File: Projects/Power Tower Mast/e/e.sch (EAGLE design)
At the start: 25 parts

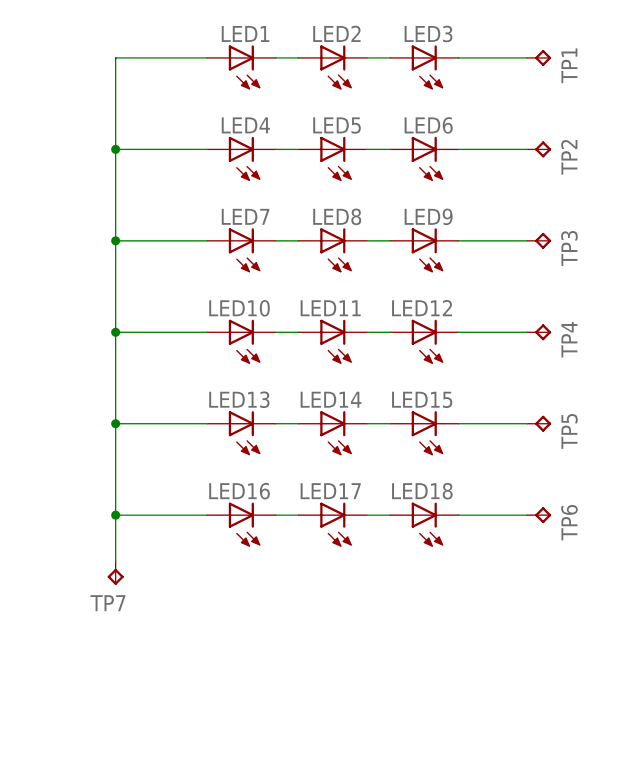
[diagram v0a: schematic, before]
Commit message: updated with extra vias and panelized
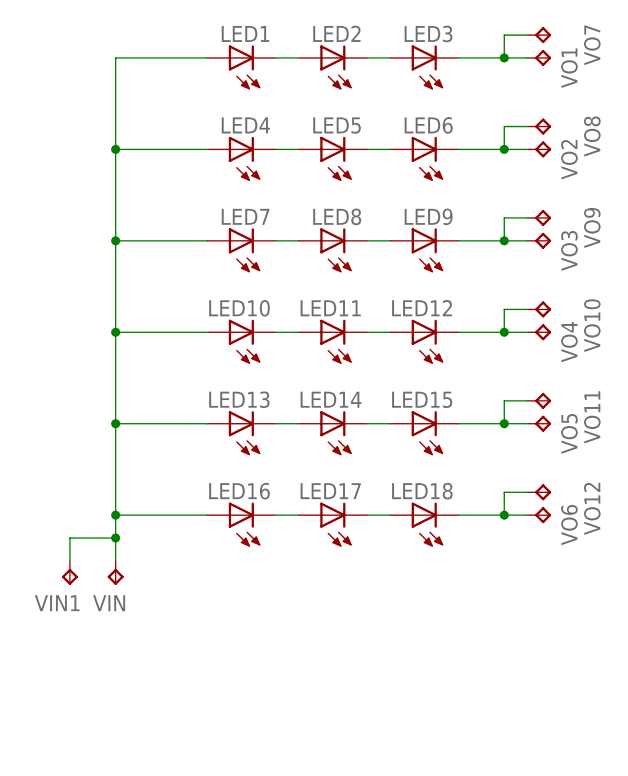
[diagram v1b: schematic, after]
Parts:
- added VIN1, VO10, VO11, VO12, VO7, VO8, VO9: (no value), CyberRailGuru:TEST_POINTPAD1-20
- renumbered TP1 to VO1, TP2 to VO2, TP3 to VO3, TP4 to VO4, TP5 to VO5, TP6 to VO6, TP7 to VIN
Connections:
- removed net VIN4: LED1.A, LED10.A, LED13.A, LED16.A, LED4.A, LED7.A, VIN.TP
- removed net VOUT20: LED3.C, VO1.TP
- removed net VOUT21: LED6.C, VO2.TP
- removed net VOUT22: LED9.C, VO3.TP
- removed net VOUT23: LED12.C, VO4.TP
- removed net VOUT24: LED15.C, VO5.TP
- removed net VOUT25: LED18.C, VO6.TP
- new net VIN: LED1.A, LED10.A, LED13.A, LED16.A, LED4.A, LED7.A, VIN.TP, VIN1.TP
- new net VOUT1: LED3.C, VO1.TP, VO7.TP
- new net VOUT2: LED6.C, VO2.TP, VO8.TP
- new net VOUT3: LED9.C, VO3.TP, VO9.TP
- new net VOUT4: LED12.C, VO10.TP, VO4.TP
- new net VOUT5: LED15.C, VO11.TP, VO5.TP
- new net VOUT6: LED18.C, VO12.TP, VO6.TP

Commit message: reworking some letters
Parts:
- added LED19, LED20, LED21: (no value), CyberRailGuru:LED0805
- added VO13, VO14: (no value), CyberRailGuru:TEST_POINTPAD1-20
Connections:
- new net N$1: LED19.C, LED20.A
- new net N$2: LED20.C, LED21.A
- new net N$3: LED21.C, VO14.TP, VO7.TP
- net VIN: now also LED19.A
- net VOUT1: now also VO8.TP; no longer VO7.TP
- net VOUT2: now also VO9.TP; no longer VO8.TP
- net VOUT3: now also VO10.TP; no longer VO9.TP
- net VOUT4: now also VO11.TP; no longer VO10.TP
- net VOUT5: now also VO12.TP; no longer VO11.TP
- net VOUT6: now also VO13.TP; no longer VO12.TP
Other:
- moved on the sheet: VIN, VIN1, VO10, VO11, VO12, VO7, VO8, VO9
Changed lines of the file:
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@@
 <part name="VO6" library="CyberRailGuru" deviceset="TEST_POINT" device="PAD1-20"/>
 <part name="VIN1" library="CyberRailGuru" deviceset="TEST_POINT" device="PAD1-20"/>
-<part name="VO7" library="CyberRailGuru" deviceset="TEST_POINT" device="PAD1-20"/>
 <part name="VO8" library="CyberRailGuru" deviceset="TEST_POINT" device="PAD1-20"/>
 <part name="VO9" library="CyberRailGuru" deviceset="TEST_POINT" device="PAD1-20"/>
@@
 <part name="VO11" library="CyberRailGuru" deviceset="TEST_POINT" device="PAD1-20"/>
 <part name="VO12" library="CyberRailGuru" deviceset="TEST_POINT" device="PAD1-20"/>
+<part name="VO13" library="CyberRailGuru" deviceset="TEST_POINT" device="PAD1-20"/>
+<part name="LED19" library="CyberRailGuru" deviceset="LED" device="0805"/>
+<part name="LED20" library="CyberRailGuru" deviceset="LED" device="0805"/>
+<part name="LED21" library="CyberRailGuru" deviceset="LED" device="0805"/>
+<part name="VO7" library="CyberRailGuru" deviceset="TEST_POINT" device="PAD1-20"/>
+<part name="VO14" library="CyberRailGuru" deviceset="TEST_POINT" device="PAD1-20"/>
 </parts>
 <sheets>
@@
 <instance part="LED17" gate="G$1" x="81.28" y="144.78" rot="R90"/>
 <instance part="LED16" gate="G$1" x="71.12" y="144.78" rot="R90"/>
-<instance part="VIN" gate="G$1" x="58.42" y="137.16" rot="R180"/>
+<instance part="VIN" gate="G$1" x="58.42" y="121.92" rot="R180"/>
 <instance part="VO1" gate="G$1" x="106.68" y="195.58" smashed="yes" rot="R270">
 <attribute name="NAME" x="107.95" y="196.85" size="1.778" layer="95" rot="R270"/>
@@
 <attribute name="VALUE" x="105.41" y="143.51" size="1.778" layer="96" rot="R270"/>
 </instance>
-<instance part="VIN1" gate="G$1" x="53.34" y="137.16" rot="R180"/>
-<instance part="VO7" gate="G$1" x="106.68" y="198.12" smashed="yes" rot="R270">
+<instance part="VIN1" gate="G$1" x="53.34" y="121.92" rot="R180"/>
+<instance part="VO8" gate="G$1" x="106.68" y="198.12" smashed="yes" rot="R270">
 <attribute name="NAME" x="110.49" y="199.39" size="1.778" layer="95" rot="R270"/>
 <attribute name="VALUE" x="105.41" y="196.85" size="1.778" layer="96" rot="R270"/>
 </instance>
-<instance part="VO8" gate="G$1" x="106.68" y="187.96" smashed="yes" rot="R270">
+<instance part="VO9" gate="G$1" x="106.68" y="187.96" smashed="yes" rot="R270">
 <attribute name="NAME" x="110.49" y="189.23" size="1.778" layer="95" rot="R270"/>
 <attribute name="VALUE" x="105.41" y="186.69" size="1.778" layer="96" rot="R270"/>
 </instance>
-<instance part="VO9" gate="G$1" x="106.68" y="177.8" smashed="yes" rot="R270">
+<instance part="VO10" gate="G$1" x="106.68" y="177.8" smashed="yes" rot="R270">
 <attribute name="NAME" x="110.49" y="179.07" size="1.778" layer="95" rot="R270"/>
 <attribute name="VALUE" x="105.41" y="176.53" size="1.778" layer="96" rot="R270"/>
 </instance>
-<instance part="VO10" gate="G$1" x="106.68" y="167.64" smashed="yes" rot="R270">
+<instance part="VO11" gate="G$1" x="106.68" y="167.64" smashed="yes" rot="R270">
 <attribute name="NAME" x="110.49" y="168.91" size="1.778" layer="95" rot="R270"/>
 <attribute name="VALUE" x="105.41" y="166.37" size="1.778" layer="96" rot="R270"/>
 </instance>
-<instance part="VO11" gate="G$1" x="106.68" y="157.48" smashed="yes" rot="R270">
+<instance part="VO12" gate="G$1" x="106.68" y="157.48" smashed="yes" rot="R270">
 <attribute name="NAME" x="110.49" y="158.75" size="1.778" layer="95" rot="R270"/>
 <attribute name="VALUE" x="105.41" y="156.21" size="1.778" layer="96" rot="R270"/>
 </instance>
-<instance part="VO12" gate="G$1" x="106.68" y="147.32" smashed="yes" rot="R270">
+<instance part="VO13" gate="G$1" x="106.68" y="147.32" smashed="yes" rot="R270">
 <attribute name="NAME" x="110.49" y="148.59" size="1.778" layer="95" rot="R270"/>
 <attribute name="VALUE" x="105.41" y="146.05" size="1.778" layer="96" rot="R270"/>
+</instance>
+<instance part="LED19" gate="G$1" x="71.12" y="134.62" rot="R90"/>
+<instance part="LED20" gate="G$1" x="81.28" y="134.62" rot="R90"/>
+<instance part="LED21" gate="G$1" x="91.44" y="134.62" rot="R90"/>
+<instance part="VO7" gate="G$1" x="106.68" y="134.62" smashed="yes" rot="R270">
+<attribute name="NAME" x="107.95" y="135.89" size="1.778" layer="95" rot="R270"/>
+<attribute name="VALUE" x="105.41" y="133.35" size="1.778" layer="96" rot="R270"/>
+</instance>
+<instance part="VO14" gate="G$1" x="106.68" y="137.16" smashed="yes" rot="R270">
+<attribute name="NAME" x="110.49" y="138.43" size="1.778" layer="95" rot="R270"/>
+<attribute name="VALUE" x="105.41" y="135.89" size="1.778" layer="96" rot="R270"/>
 </instance>
 </instances>
@@
 <wire x1="96.52" y1="195.58" x2="101.6" y2="195.58" width="0.1524" layer="91"/>
 <pinref part="VO1" gate="G$1" pin="TP"/>
-<pinref part="VO7" gate="G$1" pin="TP"/>
+<pinref part="VO8" gate="G$1" pin="TP"/>
 <wire x1="101.6" y1="195.58" x2="104.14" y2="195.58" width="0.1524" layer="91"/>
 <wire x1="104.14" y1="198.12" x2="101.6" y2="198.12" width="0.1524" layer="91"/>
@@
 <wire x1="96.52" y1="185.42" x2="101.6" y2="185.42" width="0.1524" layer="91"/>
 <pinref part="VO2" gate="G$1" pin="TP"/>
-<pinref part="VO8" gate="G$1" pin="TP"/>
+<pinref part="VO9" gate="G$1" pin="TP"/>
 <wire x1="101.6" y1="185.42" x2="104.14" y2="185.42" width="0.1524" layer="91"/>
 <wire x1="104.14" y1="187.96" x2="101.6" y2="187.96" width="0.1524" layer="91"/>
@@
 <wire x1="96.52" y1="175.26" x2="101.6" y2="175.26" width="0.1524" layer="91"/>
 <pinref part="VO3" gate="G$1" pin="TP"/>
-<pinref part="VO9" gate="G$1" pin="TP"/>
+<pinref part="VO10" gate="G$1" pin="TP"/>
 <wire x1="101.6" y1="175.26" x2="104.14" y2="175.26" width="0.1524" layer="91"/>
 <wire x1="104.14" y1="177.8" x2="101.6" y2="177.8" width="0.1524" layer="91"/>
@@
 <wire x1="96.52" y1="165.1" x2="101.6" y2="165.1" width="0.1524" layer="91"/>
 <pinref part="VO4" gate="G$1" pin="TP"/>
-<pinref part="VO10" gate="G$1" pin="TP"/>
+<pinref part="VO11" gate="G$1" pin="TP"/>
 <wire x1="101.6" y1="165.1" x2="104.14" y2="165.1" width="0.1524" layer="91"/>
 <wire x1="104.14" y1="167.64" x2="101.6" y2="167.64" width="0.1524" layer="91"/>
@@
 <wire x1="96.52" y1="154.94" x2="101.6" y2="154.94" width="0.1524" layer="91"/>
 <pinref part="VO5" gate="G$1" pin="TP"/>
-<pinref part="VO11" gate="G$1" pin="TP"/>
+<pinref part="VO12" gate="G$1" pin="TP"/>
 <wire x1="101.6" y1="154.94" x2="104.14" y2="154.94" width="0.1524" layer="91"/>
 <wire x1="104.14" y1="157.48" x2="101.6" y2="157.48" width="0.1524" layer="91"/>
@@
 <wire x1="96.52" y1="144.78" x2="101.6" y2="144.78" width="0.1524" layer="91"/>
 <pinref part="VO6" gate="G$1" pin="TP"/>
-<pinref part="VO12" gate="G$1" pin="TP"/>
+<pinref part="VO13" gate="G$1" pin="TP"/>
 <wire x1="101.6" y1="144.78" x2="104.14" y2="144.78" width="0.1524" layer="91"/>
 <wire x1="104.14" y1="147.32" x2="101.6" y2="147.32" width="0.1524" layer="91"/>
@@
 <wire x1="58.42" y1="165.1" x2="58.42" y2="154.94" width="0.1524" layer="91"/>
 <wire x1="58.42" y1="154.94" x2="58.42" y2="144.78" width="0.1524" layer="91"/>
-<wire x1="58.42" y1="144.78" x2="58.42" y2="142.24" width="0.1524" layer="91"/>
+<wire x1="58.42" y1="144.78" x2="58.42" y2="134.62" width="0.1524" layer="91"/>
 <pinref part="LED16" gate="G$1" pin="A"/>
-<wire x1="58.42" y1="142.24" x2="58.42" y2="139.7" width="0.1524" layer="91"/>
+<wire x1="58.42" y1="134.62" x2="58.42" y2="127" width="0.1524" layer="91"/>
+<wire x1="58.42" y1="127" x2="58.42" y2="124.46" width="0.1524" layer="91"/>
 <wire x1="58.42" y1="144.78" x2="68.58" y2="144.78" width="0.1524" layer="91"/>
 <pinref part="LED13" gate="G$1" pin="A"/>
@@
 <pinref part="VIN" gate="G$1" pin="TP"/>
 <pinref part="VIN1" gate="G$1" pin="TP"/>
-<wire x1="53.34" y1="139.7" x2="53.34" y2="142.24" width="0.1524" layer="91"/>
-<wire x1="53.34" y1="142.24" x2="58.42" y2="142.24" width="0.1524" layer="91"/>
-<junction x="58.42" y="142.24"/>
-</segment>
-</net>
+<wire x1="53.34" y1="124.46" x2="53.34" y2="127" width="0.1524" layer="91"/>
+<wire x1="53.34" y1="127" x2="58.42" y2="127" width="0.1524" layer="91"/>
+<junction x="58.42" y="127"/>
+<pinref part="LED19" gate="G$1" pin="A"/>
+<wire x1="68.58" y1="134.62" x2="58.42" y2="134.62" width="0.1524" layer="91"/>
+<junction x="58.42" y="134.62"/>
+</segment>
+</net>
+<net name="N$1" class="0">
+<segment>
+<pinref part="LED19" gate="G$1" pin="C"/>
+<pinref part="LED20" gate="G$1" pin="A"/>
+<wire x1="76.2" y1="134.62" x2="78.74" y2="134.62" width="0.1524" layer="91"/>
+</segment>
+</net>
+<net name="N$2" class="0">
+<segment>
+<pinref part="LED20" gate="G$1" pin="C"/>
+<pinref part="LED21" gate="G$1" pin="A"/>
+<wire x1="86.36" y1="134.62" x2="88.9" y2="134.62" width="0.1524" layer="91"/>
+</segment>
+</net>
+<net name="N$3" class="0">
+<segment>
+<pinref part="LED21" gate="G$1" pin="C"/>
+<pinref part="VO7" gate="G$1" pin="TP"/>
+<wire x1="96.52" y1="134.62" x2="101.6" y2="134.62" width="0.1524" layer="91"/>
+<pinref part="VO14" gate="G$1" pin="TP"/>
+<wire x1="101.6" y1="134.62" x2="104.14" y2="134.62" width="0.1524" layer="91"/>
+<wire x1="104.14" y1="137.16" x2="101.6" y2="137.16" width="0.1524" layer="91"/>
+<wire x1="101.6" y1="137.16" x2="101.6" y2="134.62" width="0.1524" layer="91"/>
+<junction x="101.6" y="134.62"/>
+</segment>
+</net>
